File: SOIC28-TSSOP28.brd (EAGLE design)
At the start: 20 x 38.1 mm, 7 parts

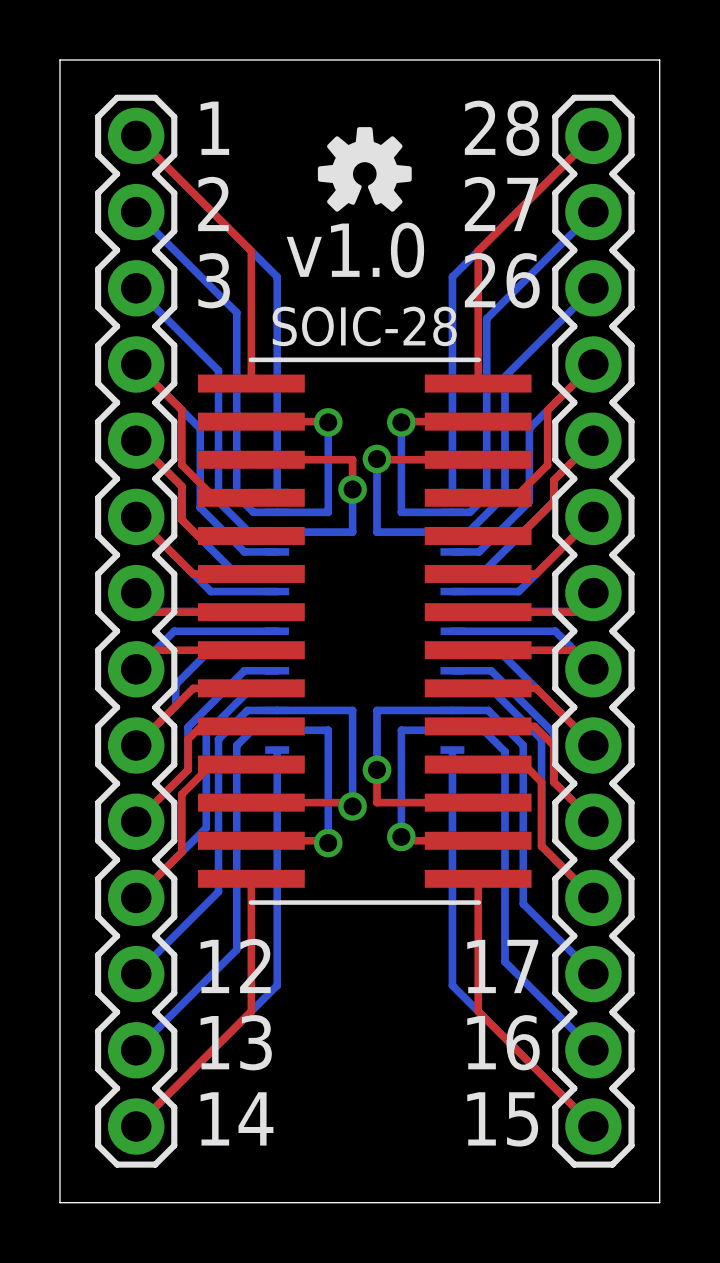
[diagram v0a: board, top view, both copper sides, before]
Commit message: Silk and board revision
Worked several silk screen issues and narrowed some boards.
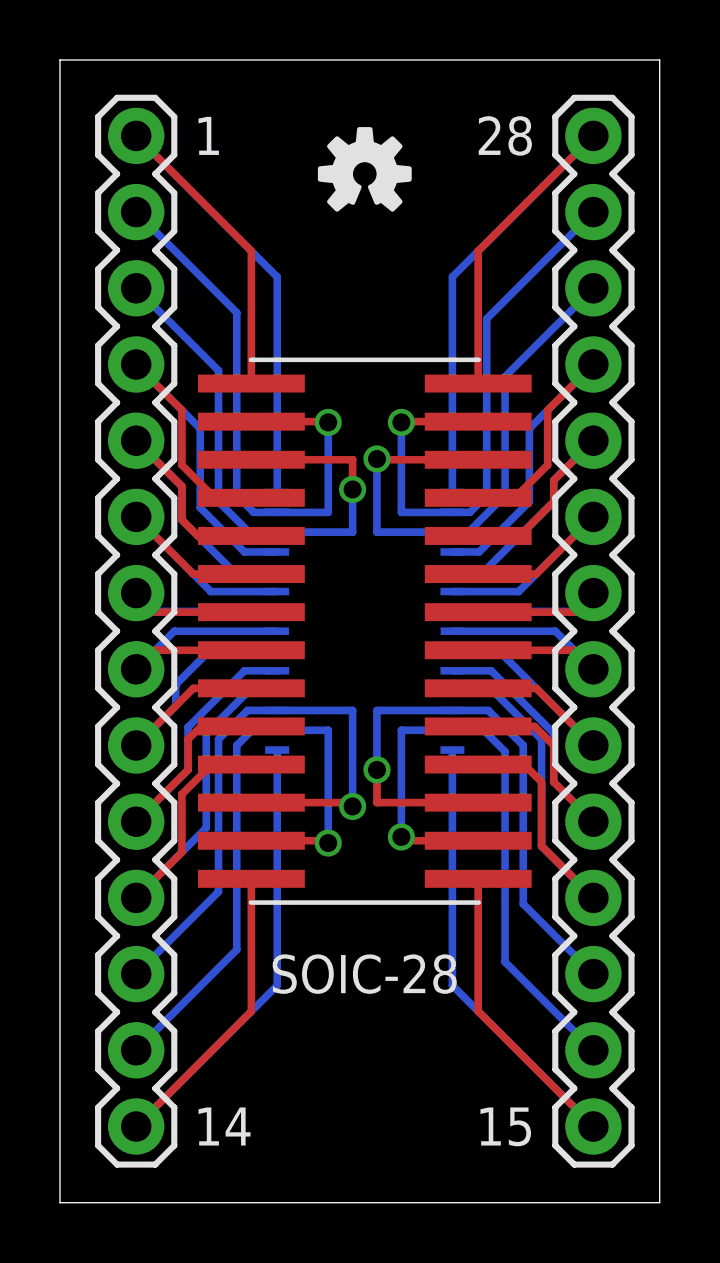
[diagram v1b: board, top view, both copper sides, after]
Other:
- board text removed: "10"
- board text removed: "11"
- board text removed: "12"
- board text removed: "13"
- board text removed: "16"
- board text removed: "17"
- board text removed: "18"
- board text removed: "19"
- board text removed: "2"
- board text removed: "20"
- board text removed: "21"
- board text removed: "22"
- board text removed: "23"
- board text removed: "24"
- board text removed: "25"
- board text removed: "26"
- board text removed: "27"
- board text removed: "3"
- board text removed: "4"
- board text removed: "5"
- board text removed: "6"
- board text removed: "7"
- board text removed: "8"
- board text removed: "9"
- board text removed: "v1.0"
